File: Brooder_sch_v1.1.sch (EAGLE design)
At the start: 26 parts, among them J1 DCJ0202, J2 1X2-3.5MM, U1 328P

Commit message: Removes four of the six ds18b20 sensor connector
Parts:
- removed R3, R4: 10k, SparkFun-Resistors:10MOHM-HORIZ-1/4W-5%
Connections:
- net 5V: no longer R3.2, R4.2
- net PB0: no longer R4.1
- net PB1: no longer R3.1
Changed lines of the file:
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@@
 <part name="DHT22_1" library="SparkFun-Connectors" deviceset="CONN_03" device="" value="dht22_1"/>
 <part name="DHT22_2" library="SparkFun-Connectors" deviceset="CONN_03" device="" value="455-1750-1-ND"/>
-<part name="R3" library="SparkFun-Resistors" deviceset="10MOHM" device="-HORIZ-1/4W-5%" value="10k"/>
-<part name="R4" library="SparkFun-Resistors" deviceset="10MOHM" device="-HORIZ-1/4W-5%" value="10k"/>
 <part name="GND10" library="supply1" library_urn="urn:adsk.eagle:library:371" deviceset="GND" device=""/>
 <part name="GND11" library="supply1" library_urn="urn:adsk.eagle:library:371" deviceset="GND" device=""/>
@@
 <attribute name="NAME" x="162.56" y="90.932" size="1.778" layer="95" font="vector" rot="R180"/>
 </instance>
-<instance part="R3" gate="G$1" x="101.6" y="104.14" smashed="yes" rot="R90">
-<attribute name="NAME" x="100.076" y="104.14" size="1.778" layer="95" font="vector" rot="R90" align="bottom-center"/>
-<attribute name="VALUE" x="103.124" y="104.14" size="1.778" layer="96" font="vector" rot="R90" align="top-center"/>
-</instance>
-<instance part="R4" gate="G$1" x="142.24" y="104.14" smashed="yes" rot="R90">
-<attribute name="NAME" x="140.716" y="104.14" size="1.778" layer="95" font="vector" rot="R90" align="bottom-center"/>
-<attribute name="VALUE" x="143.764" y="104.14" size="1.778" layer="96" font="vector" rot="R90" align="top-center"/>
-</instance>
 <instance part="GND10" gate="1" x="106.68" y="88.9" smashed="yes">
 <attribute name="VALUE" x="104.14" y="86.36" size="1.778" layer="96"/>
@@
 </segment>
 <segment>
-<pinref part="R3" gate="G$1" pin="2"/>
-<wire x1="101.6" y1="109.22" x2="101.6" y2="111.76" width="0.1524" layer="91"/>
-<label x="101.6" y="111.76" size="1.778" layer="95" rot="R90"/>
-</segment>
-<segment>
 <pinref part="DHT22_1" gate="J$1" pin="1"/>
 <wire x1="111.76" y1="99.06" x2="106.68" y2="99.06" width="0.1524" layer="91"/>
 <wire x1="106.68" y1="99.06" x2="106.68" y2="104.14" width="0.1524" layer="91"/>
 <label x="106.68" y="104.14" size="1.778" layer="95"/>
-</segment>
-<segment>
-<pinref part="R4" gate="G$1" pin="2"/>
-<wire x1="142.24" y1="109.22" x2="142.24" y2="111.76" width="0.1524" layer="91"/>
-<label x="142.24" y="111.76" size="1.778" layer="95" rot="R90"/>
 </segment>
 <segment>
@@
 <segment>
 <pinref part="DHT22_2" gate="J$1" pin="2"/>
-<wire x1="152.4" y1="96.52" x2="142.24" y2="96.52" width="0.1524" layer="91"/>
-<pinref part="R4" gate="G$1" pin="1"/>
-<wire x1="142.24" y1="96.52" x2="142.24" y2="99.06" width="0.1524" layer="91"/>
-<wire x1="142.24" y1="96.52" x2="137.16" y2="96.52" width="0.1524" layer="91"/>
-<junction x="142.24" y="96.52"/>
+<wire x1="152.4" y1="96.52" x2="137.16" y2="96.52" width="0.1524" layer="91"/>
 <label x="137.16" y="96.52" size="1.778" layer="95"/>
 </segment>
@@
 <segment>
 <pinref part="DHT22_1" gate="J$1" pin="2"/>
-<wire x1="111.76" y1="96.52" x2="101.6" y2="96.52" width="0.1524" layer="91"/>
-<pinref part="R3" gate="G$1" pin="1"/>
-<wire x1="101.6" y1="96.52" x2="91.44" y2="96.52" width="0.1524" layer="91"/>
-<wire x1="101.6" y1="99.06" x2="101.6" y2="96.52" width="0.1524" layer="91"/>
-<junction x="101.6" y="96.52"/>
+<wire x1="111.76" y1="96.52" x2="91.44" y2="96.52" width="0.1524" layer="91"/>
 <label x="91.44" y="96.52" size="1.778" layer="95"/>
 </segment>

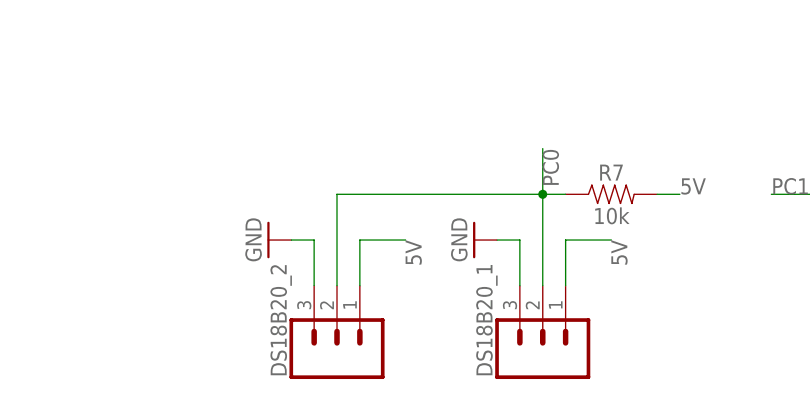
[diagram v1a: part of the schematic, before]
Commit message: Removes the dht22 resistors
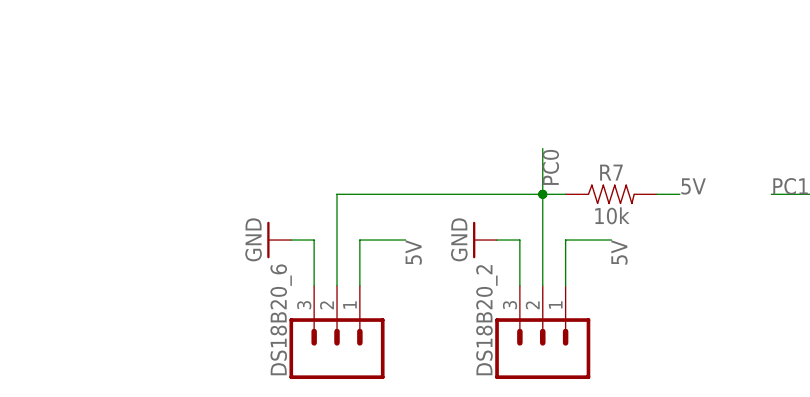
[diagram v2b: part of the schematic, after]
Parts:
- removed DS18B20_1: 455-1750-1-ND, SparkFun-Connectors:CONN_03
- added DS18B20_6: 455-1750-1-ND, SparkFun-Connectors:CONN_03
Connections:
- net 5V: now also DS18B20_6.1; no longer DS18B20_1.1
- net GND: now also DS18B20_6.3; no longer DS18B20_1.3
- net PC0: now also DS18B20_6.2; no longer DS18B20_1.2
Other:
- moved on the sheet: DS18B20_2
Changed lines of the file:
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@@
 <part name="DS18B20_2" library="SparkFun-Connectors" deviceset="CONN_03" device="" value="455-1750-1-ND"/>
 <part name="GND19" library="supply1" library_urn="urn:adsk.eagle:library:371" deviceset="GND" device=""/>
-<part name="DS18B20_1" library="SparkFun-Connectors" deviceset="CONN_03" device="" value="455-1750-1-ND"/>
 <part name="R7" library="SparkFun-Resistors" deviceset="10MOHM" device="-HORIZ-1/4W-5%" value="10k"/>
-<part name="GND20" library="supply1" library_urn="urn:adsk.eagle:library:371" deviceset="GND" device=""/>
+<part name="DS18B20_6" library="SparkFun-Connectors" deviceset="CONN_03" device="" value="455-1750-1-ND"/>
+<part name="GND23" library="supply1" library_urn="urn:adsk.eagle:library:371" deviceset="GND" device=""/>
 <part name="GND18" library="supply1" library_urn="urn:adsk.eagle:library:371" deviceset="GND" device=""/>
 <part name="J2" library="adafruit" deviceset="1X2" device="-3.5MM"/>
@@
 <attribute name="VALUE" x="24.384" y="107.061" size="1.778" layer="96" font="vector"/>
 </instance>
-<instance part="DS18B20_2" gate="J$1" x="45.72" y="-2.54" smashed="yes" rot="R90">
-<attribute name="NAME" x="40.132" y="-5.08" size="1.778" layer="95" font="vector" rot="R90"/>
-</instance>
-<instance part="GND19" gate="1" x="38.1" y="10.16" smashed="yes" rot="R270">
-<attribute name="VALUE" x="35.56" y="12.7" size="1.778" layer="96" rot="R270"/>
-</instance>
-<instance part="DS18B20_1" gate="J$1" x="68.58" y="-2.54" smashed="yes" rot="R90">
+<instance part="DS18B20_2" gate="J$1" x="68.58" y="-2.54" smashed="yes" rot="R90">
 <attribute name="NAME" x="62.992" y="-5.08" size="1.778" layer="95" font="vector" rot="R90"/>
+</instance>
+<instance part="GND19" gate="1" x="60.96" y="10.16" smashed="yes" rot="R270">
+<attribute name="VALUE" x="58.42" y="12.7" size="1.778" layer="96" rot="R270"/>
 </instance>
 <instance part="R7" gate="G$1" x="76.2" y="15.24" smashed="yes">
@@
 <attribute name="VALUE" x="76.2" y="13.716" size="1.778" layer="96" font="vector" align="top-center"/>
 </instance>
-<instance part="GND20" gate="1" x="60.96" y="10.16" smashed="yes" rot="R270">
-<attribute name="VALUE" x="58.42" y="12.7" size="1.778" layer="96" rot="R270"/>
+<instance part="DS18B20_6" gate="J$1" x="45.72" y="-2.54" smashed="yes" rot="R90">
+<attribute name="NAME" x="40.132" y="-5.08" size="1.778" layer="95" font="vector" rot="R90"/>
+</instance>
+<instance part="GND23" gate="1" x="38.1" y="10.16" smashed="yes" rot="R270">
+<attribute name="VALUE" x="35.56" y="12.7" size="1.778" layer="96" rot="R270"/>
 </instance>
 <instance part="GND18" gate="1" x="137.16" y="12.7" smashed="yes">
@@
 <segment>
 <pinref part="DS18B20_2" gate="J$1" pin="3"/>
+<wire x1="66.04" y1="5.08" x2="66.04" y2="10.16" width="0.1524" layer="91"/>
+<wire x1="66.04" y1="10.16" x2="63.5" y2="10.16" width="0.1524" layer="91"/>
+<pinref part="GND19" gate="1" pin="GND"/>
+</segment>
+<segment>
+<pinref part="DS18B20_6" gate="J$1" pin="3"/>
 <wire x1="43.18" y1="5.08" x2="43.18" y2="10.16" width="0.1524" layer="91"/>
 <wire x1="43.18" y1="10.16" x2="40.64" y2="10.16" width="0.1524" layer="91"/>
-<pinref part="GND19" gate="1" pin="GND"/>
-</segment>
-<segment>
-<pinref part="DS18B20_1" gate="J$1" pin="3"/>
-<wire x1="66.04" y1="5.08" x2="66.04" y2="10.16" width="0.1524" layer="91"/>
-<wire x1="66.04" y1="10.16" x2="63.5" y2="10.16" width="0.1524" layer="91"/>
-<pinref part="GND20" gate="1" pin="GND"/>
+<pinref part="GND23" gate="1" pin="GND"/>
 </segment>
 <segment>
@@
 <segment>
 <pinref part="DS18B20_2" gate="J$1" pin="1"/>
+<wire x1="71.12" y1="5.08" x2="71.12" y2="10.16" width="0.1524" layer="91"/>
+<wire x1="71.12" y1="10.16" x2="76.2" y2="10.16" width="0.1524" layer="91"/>
+<label x="76.2" y="10.16" size="1.778" layer="95" rot="R270"/>
+</segment>
+<segment>
+<pinref part="R7" gate="G$1" pin="2"/>
+<wire x1="81.28" y1="15.24" x2="83.82" y2="15.24" width="0.1524" layer="91"/>
+<label x="83.82" y="15.24" size="1.778" layer="95"/>
+</segment>
+<segment>
+<pinref part="DS18B20_6" gate="J$1" pin="1"/>
 <wire x1="48.26" y1="5.08" x2="48.26" y2="10.16" width="0.1524" layer="91"/>
 <wire x1="48.26" y1="10.16" x2="53.34" y2="10.16" width="0.1524" layer="91"/>
 <label x="53.34" y="10.16" size="1.778" layer="95" rot="R270"/>
-</segment>
-<segment>
-<pinref part="R7" gate="G$1" pin="2"/>
-<wire x1="81.28" y1="15.24" x2="83.82" y2="15.24" width="0.1524" layer="91"/>
-<label x="83.82" y="15.24" size="1.778" layer="95"/>
-</segment>
-<segment>
-<pinref part="DS18B20_1" gate="J$1" pin="1"/>
-<wire x1="71.12" y1="5.08" x2="71.12" y2="10.16" width="0.1524" layer="91"/>
-<wire x1="71.12" y1="10.16" x2="76.2" y2="10.16" width="0.1524" layer="91"/>
-<label x="76.2" y="10.16" size="1.778" layer="95" rot="R270"/>
 </segment>
 <segment>
@@
 </segment>
 <segment>
-<pinref part="DS18B20_1" gate="J$1" pin="2"/>
-<wire x1="68.58" y1="5.08" x2="68.58" y2="15.24" width="0.1524" layer="91"/>
 <pinref part="R7" gate="G$1" pin="1"/>
 <wire x1="68.58" y1="15.24" x2="71.12" y2="15.24" width="0.1524" layer="91"/>
@@
 <label x="68.58" y="20.32" size="1.778" layer="95" rot="R270"/>
 <pinref part="DS18B20_2" gate="J$1" pin="2"/>
+<wire x1="68.58" y1="5.08" x2="68.58" y2="15.24" width="0.1524" layer="91"/>
+<junction x="68.58" y="15.24"/>
+<wire x1="45.72" y1="15.24" x2="68.58" y2="15.24" width="0.1524" layer="91"/>
+<pinref part="DS18B20_6" gate="J$1" pin="2"/>
 <wire x1="45.72" y1="5.08" x2="45.72" y2="15.24" width="0.1524" layer="91"/>
-<wire x1="45.72" y1="15.24" x2="68.58" y2="15.24" width="0.1524" layer="91"/>
-</segment>
-</net>
+</segment>
+</net>

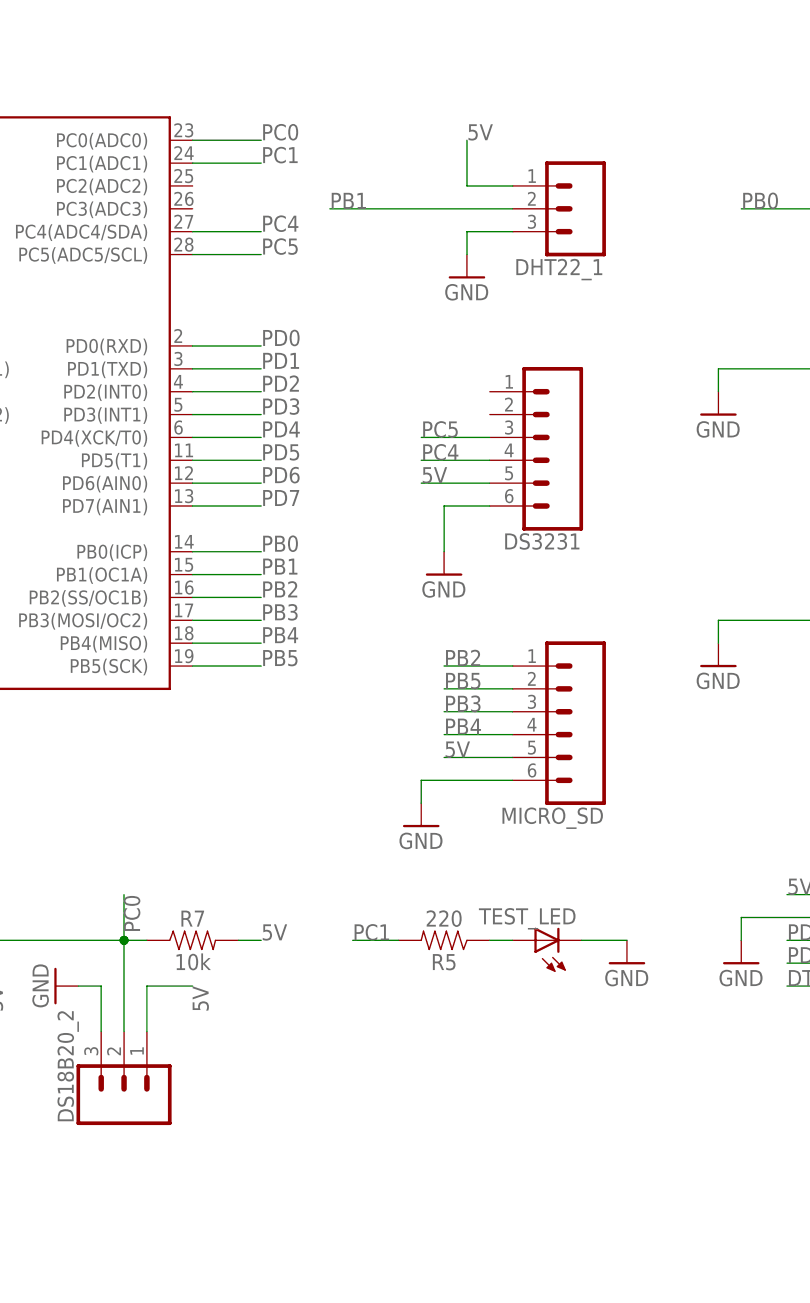
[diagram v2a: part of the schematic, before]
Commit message: Adds the sim800l V2 pin headers
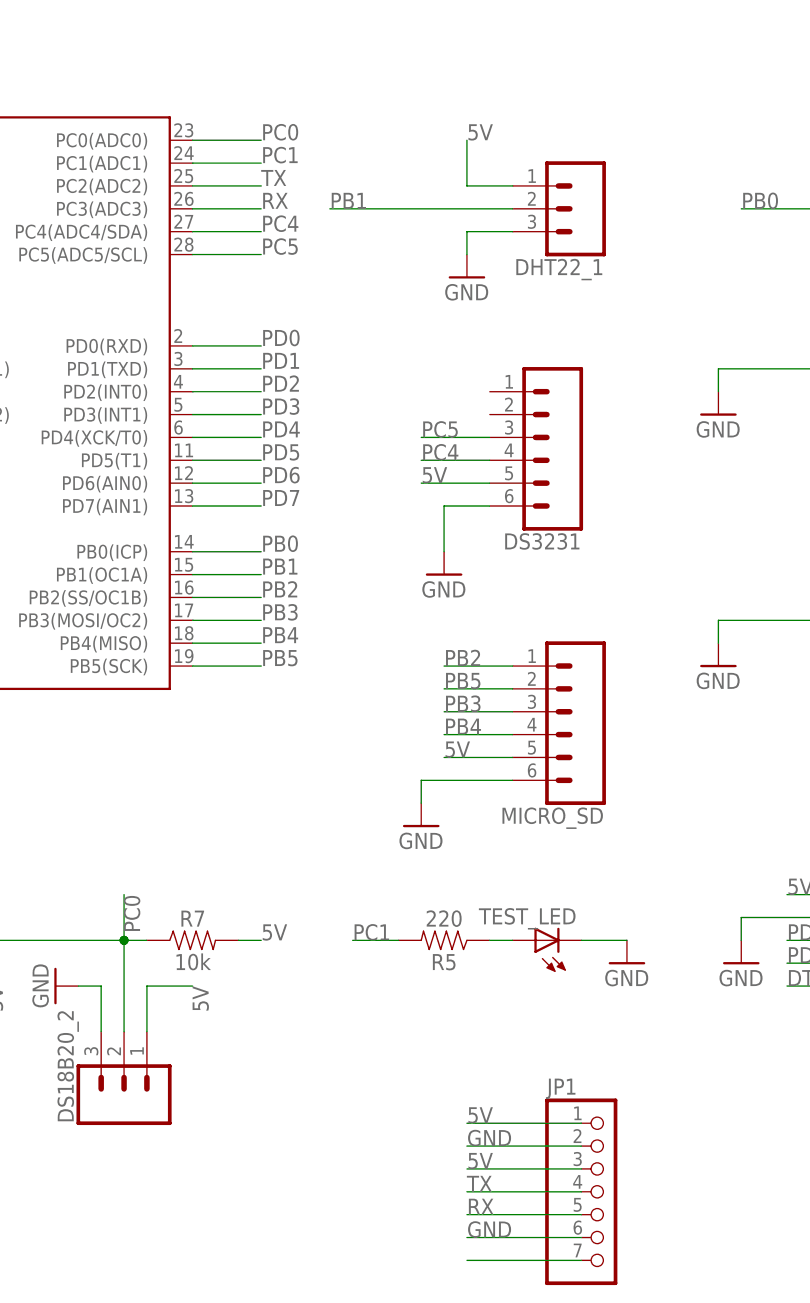
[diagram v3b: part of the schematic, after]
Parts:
- added JP1: (no value), pinhead:PINHD-1X7
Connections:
- new net N$12: JP1.7
- new net RX: JP1.5, U1.PC3(ADC3)
- new net TX: JP1.4, U1.PC2(ADC2)
- net 5V: now also JP1.1, JP1.3
- net GND: now also JP1.2, JP1.6
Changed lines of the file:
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@@
 <part name="GND25" library="supply1" library_urn="urn:adsk.eagle:library:371" deviceset="GND" device=""/>
 <part name="U$2" library="LM2596_BREAKOUT_BOARD" deviceset="LM2596_BREAKOUT_BOARD" device="THROUGH_HOLE"/>
+<part name="JP1" library="pinhead" deviceset="PINHD-1X7" device=""/>
 </parts>
 <sheets>
@@
 </instance>
 <instance part="U$2" gate="G$1" x="-20.32" y="129.54" rot="R90"/>
+<instance part="JP1" gate="A" x="121.92" y="-12.7"/>
 </instances>
 <busses>
@@
 <wire x1="104.14" y1="63.5" x2="104.14" y2="58.42" width="0.1524" layer="91"/>
 <pinref part="GND25" gate="1" pin="GND"/>
+</segment>
+<segment>
+<pinref part="JP1" gate="A" pin="2"/>
+<wire x1="119.38" y1="-7.62" x2="106.68" y2="-7.62" width="0.1524" layer="91"/>
+<label x="106.68" y="-7.62" size="1.778" layer="95"/>
+</segment>
+<segment>
+<pinref part="JP1" gate="A" pin="6"/>
+<wire x1="119.38" y1="-17.78" x2="106.68" y2="-17.78" width="0.1524" layer="91"/>
+<label x="106.68" y="-17.78" size="1.778" layer="95"/>
 </segment>
 </net>
@@
 <label x="101.6" y="66.04" size="1.778" layer="95"/>
 </segment>
+<segment>
+<pinref part="JP1" gate="A" pin="1"/>
+<wire x1="119.38" y1="-5.08" x2="106.68" y2="-5.08" width="0.1524" layer="91"/>
+<label x="106.68" y="-5.08" size="1.778" layer="95"/>
+</segment>
+<segment>
+<pinref part="JP1" gate="A" pin="3"/>
+<wire x1="119.38" y1="-10.16" x2="106.68" y2="-10.16" width="0.1524" layer="91"/>
+<label x="106.68" y="-10.16" size="1.778" layer="95"/>
+</segment>
 </net>
 <net name="N$3" class="0">
@@
 </segment>
 </net>
+<net name="TX" class="0">
+<segment>
+<pinref part="JP1" gate="A" pin="4"/>
+<wire x1="119.38" y1="-12.7" x2="106.68" y2="-12.7" width="0.1524" layer="91"/>
+<label x="106.68" y="-12.7" size="1.778" layer="95"/>
+</segment>
+<segment>
+<pinref part="U1" gate="U1" pin="PC2(ADC2)"/>
+<wire x1="76.2" y1="99.06" x2="83.82" y2="99.06" width="0.1524" layer="91"/>
+<label x="83.82" y="99.06" size="1.778" layer="95"/>
+</segment>
+</net>
+<net name="RX" class="0">
+<segment>
+<pinref part="JP1" gate="A" pin="5"/>
+<wire x1="119.38" y1="-15.24" x2="106.68" y2="-15.24" width="0.1524" layer="91"/>
+<label x="106.68" y="-15.24" size="1.778" layer="95"/>
+</segment>
+<segment>
+<pinref part="U1" gate="U1" pin="PC3(ADC3)"/>
+<wire x1="76.2" y1="96.52" x2="83.82" y2="96.52" width="0.1524" layer="91"/>
+<label x="83.82" y="96.52" size="1.778" layer="95"/>
+</segment>
+</net>
+<net name="N$12" class="0">
+<segment>
+<pinref part="JP1" gate="A" pin="7"/>
+<wire x1="119.38" y1="-20.32" x2="106.68" y2="-20.32" width="0.1524" layer="91"/>
+</segment>
+</net>

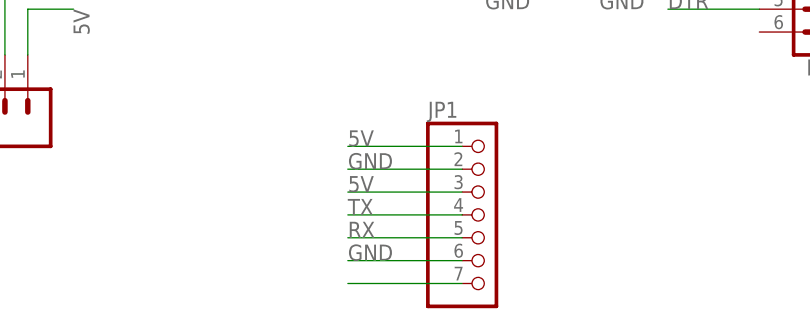
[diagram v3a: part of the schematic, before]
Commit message: Adds the sim800 to the PCB board
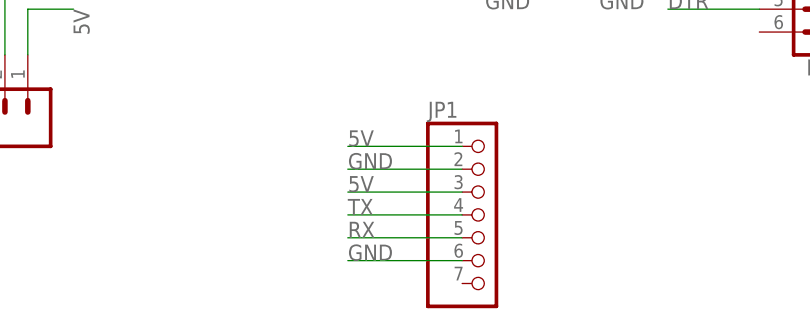
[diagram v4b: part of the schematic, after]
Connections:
- removed net N$12: JP1.7
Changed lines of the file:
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@@
-</segment>
-</net>
-<net name="N$12" class="0">
-<segment>
-<pinref part="JP1" gate="A" pin="7"/>
-<wire x1="119.38" y1="-20.32" x2="106.68" y2="-20.32" width="0.1524" layer="91"/>
 </segment>
 </net>
